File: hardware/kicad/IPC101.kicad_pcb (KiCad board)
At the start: 2 copper layers, 100 x 140 mm, 18 parts, among them J1 IPC-100 J10, J3 STOP J8A ONLY, SW1 START, SW2 PULL, SW3 NAV 5-WAY - VERIFY, U1 TCA8418RTWR

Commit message: Update IPC-101 for 2.42-inch OLED
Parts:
- removed DS1: ADAFRUIT 938 - J6 HARNESS, IPC101:OLED_MOUNT
- C1: value 100n -> 100nF
- C2: value 4.7u -> 4.7uF
- J3: value STOP J8A ONLY -> IPC-100 J8A STOP
- SW1: value START -> START B3F-4055
- SW2: value PULL -> PULL B3F-4055
- SW3: value NAV 5-WAY - VERIFY -> ADAFRUIT 504 - VERIFY PIN MAP
- TP1: value 3V3 -> +3V3
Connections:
- net +3V3 renamed /+3V3
- net C0 renamed /C0
- net GND renamed /GND
- net INT_TEST renamed /INT_TEST
- net R0_LEFT renamed /R0_LEFT
- net R1_RIGHT renamed /R1_RIGHT
- net R2_UP renamed /R2_UP
- net R3_DOWN renamed /R3_DOWN
- net R4_SELECT renamed /R4_SELECT
- net R5_START renamed /R5_START
- net R6_PULL renamed /R6_PULL
- net RESET renamed /RESET
- net SCL renamed /SCL
- net SDA renamed /SDA
- net STOP_IN_RAW renamed /STOP_IN_RAW
- net STOP_RETURN renamed /STOP_RETURN
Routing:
- net (no net): track 0.00 -> 430.0 mm
- net /C0: track 86.9 -> 0.00 mm
- net /SCL: track 66.3 -> 0.00 mm
- net /SDA: track 66.2 -> 0.00 mm
- net /+3V3: track 60.2 -> 0.00 mm
- net /R6_PULL: track 43.4 -> 0.00 mm
- net /R5_START: track 29.0 -> 0.00 mm
- net /R2_UP: track 19.4 -> 0.00 mm
- net /R1_RIGHT: track 16.4 -> 0.00 mm
- net /R0_LEFT: track 15.8 -> 0.00 mm
- net /R4_SELECT: track 11.0 -> 0.00 mm
- net /R3_DOWN: track 9.19 -> 0.00 mm
- net /GND: track 6.22 -> 0.00 mm

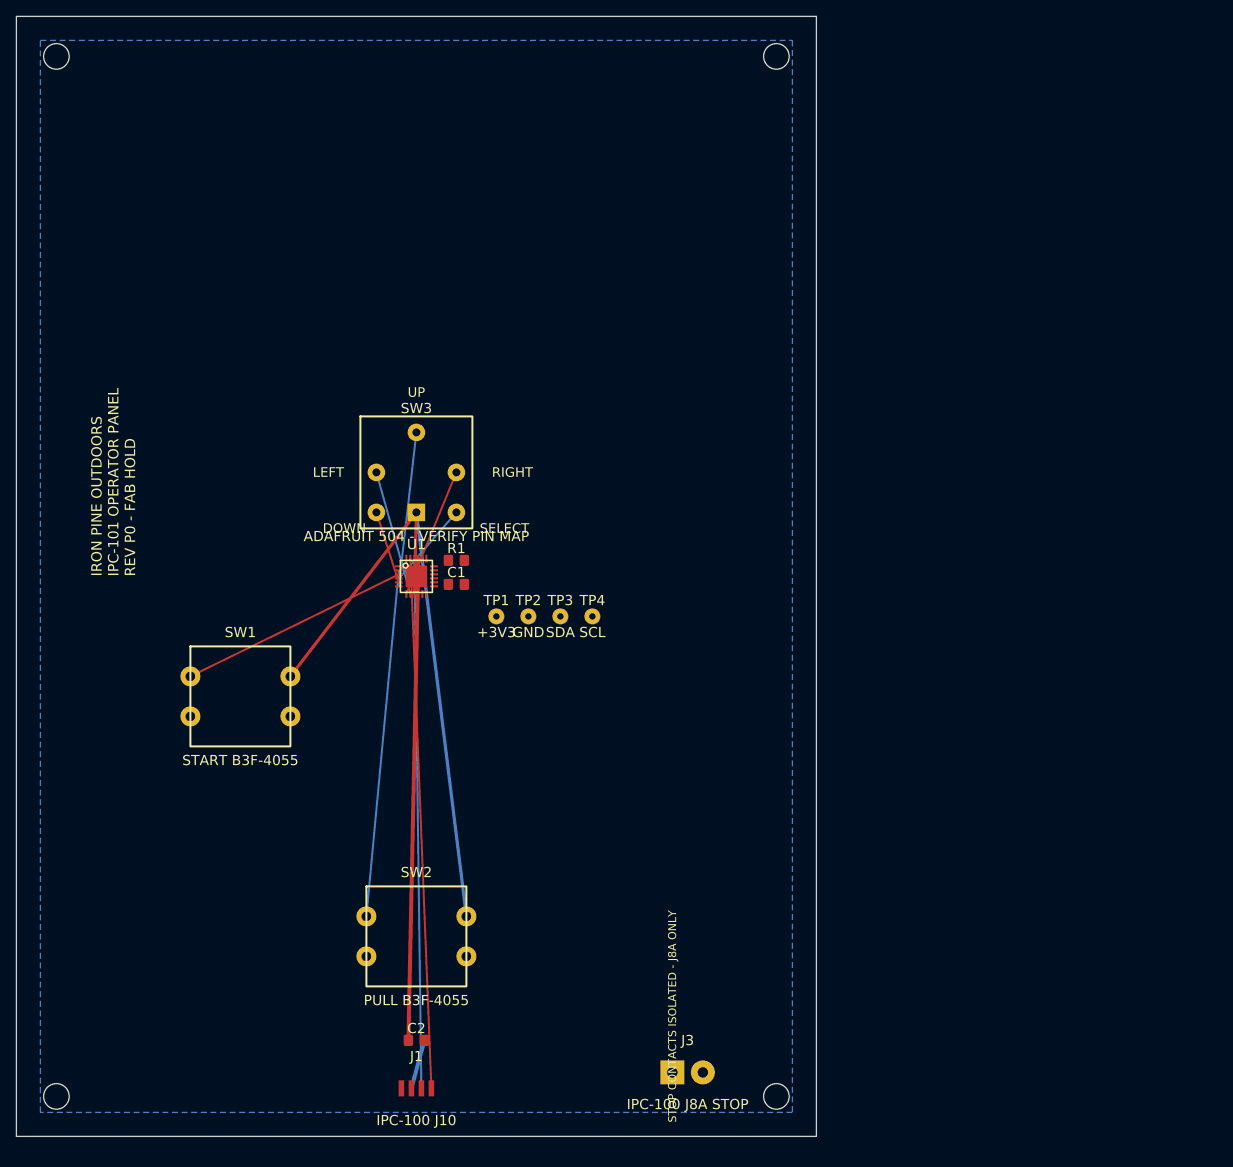
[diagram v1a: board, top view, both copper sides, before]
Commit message: Repair IPC-101 PCB routing
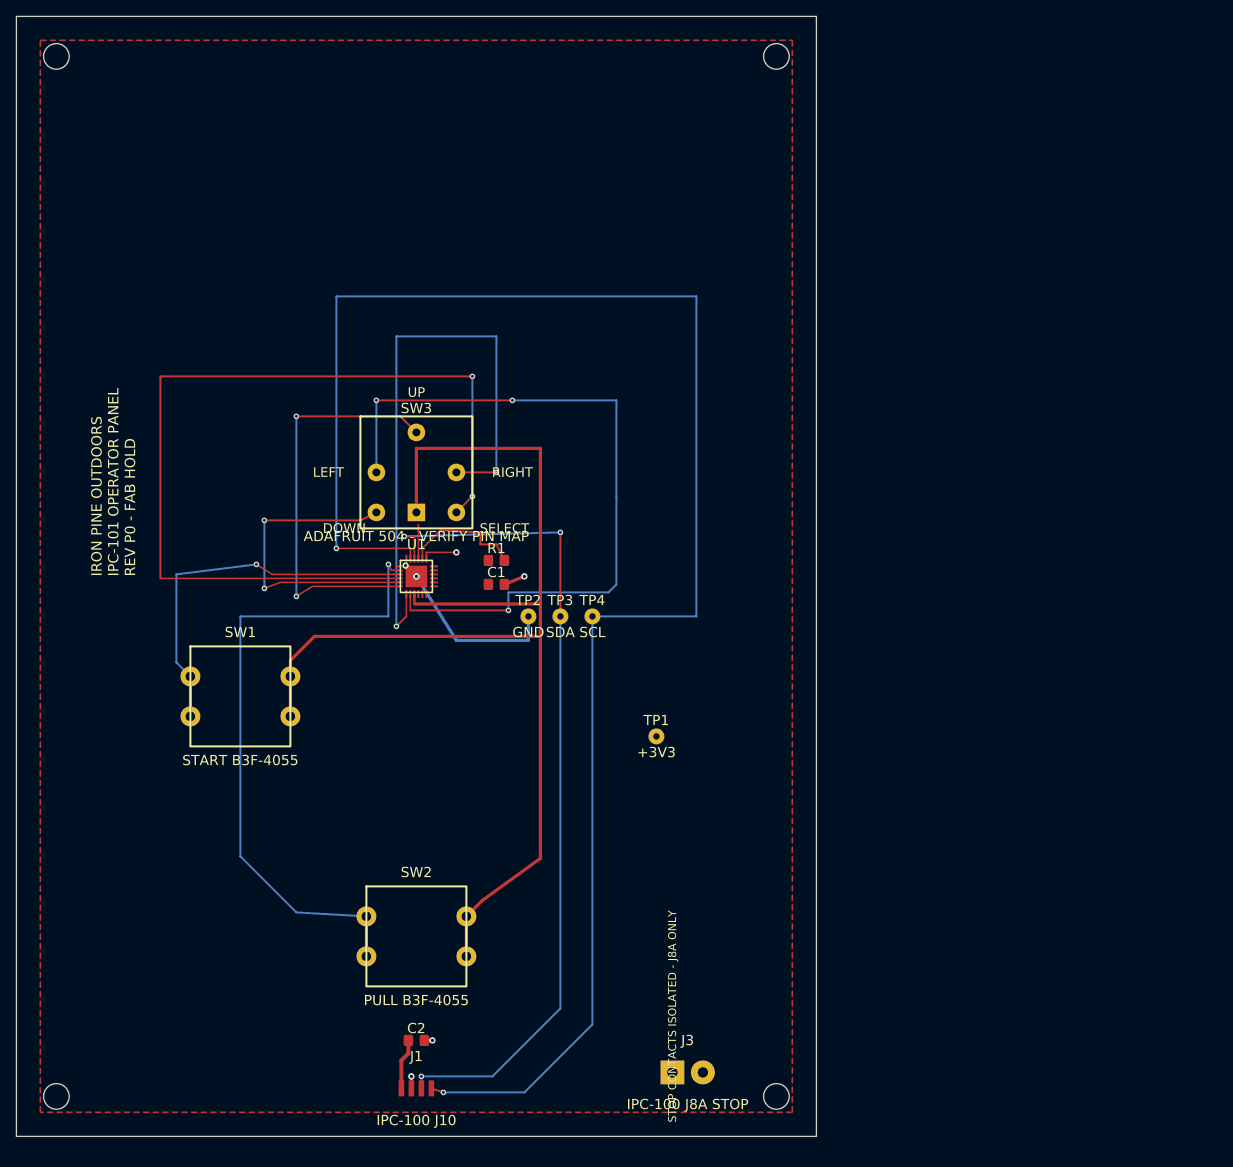
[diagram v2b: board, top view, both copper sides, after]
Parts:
- moved TP1 25.0 mm to (80.0, 90.0)
- moved C1 5.00 mm to (60.0, 71.0)
- moved R1 5.00 mm to (60.0, 68.0)
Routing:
- net (no net): track 430.0 -> 0.00 mm
- net /SCL: track 0.00 -> 214.8 mm, vias 0 -> 2
- net /C0: track 0.00 -> 148.0 mm
- net /R4_SELECT: track 0.00 -> 111.9 mm, vias 0 -> 2
- net /SDA: track 0.00 -> 105.5 mm, vias 0 -> 3
- net /R0_LEFT: track 0.00 -> 92.5 mm, vias 0 -> 3
- net /R6_PULL: track 0.00 -> 80.4 mm, vias 0 -> 1
- net /R1_RIGHT: track 0.00 -> 75.3 mm, vias 0 -> 2
- net /R2_UP: track 0.00 -> 51.5 mm, vias 0 -> 2
- net /R5_START: track 0.00 -> 46.7 mm, vias 0 -> 1
- net /R3_DOWN: track 0.00 -> 39.7 mm, vias 0 -> 2
- net /GND: track 0.00 -> 31.2 mm, vias 0 -> 5
- net /RESET: track 0.00 -> 15.2 mm
- net /+3V3: track 0.00 -> 10.7 mm
- added copper zone on F.Cu, net /+3V3

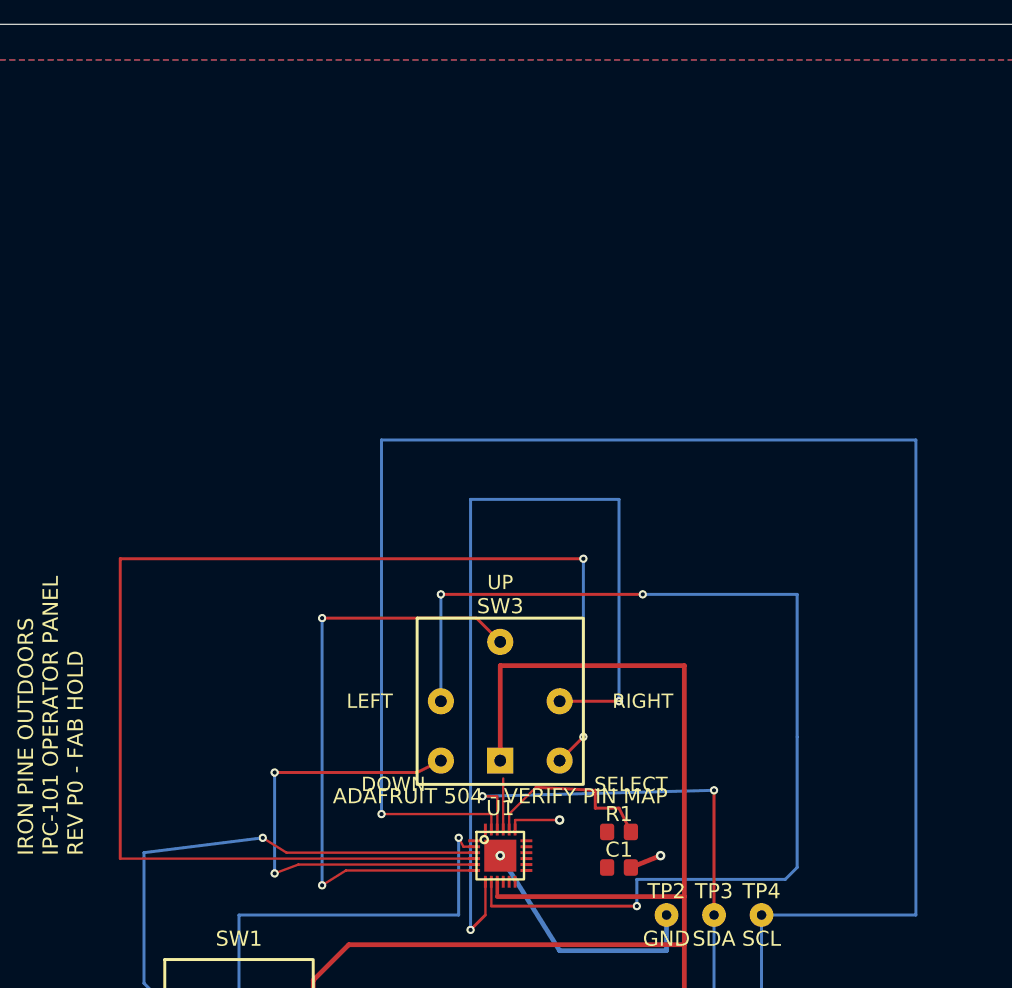
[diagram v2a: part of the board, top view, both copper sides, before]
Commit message: Mount 2.42 inch OLED on IPC-101
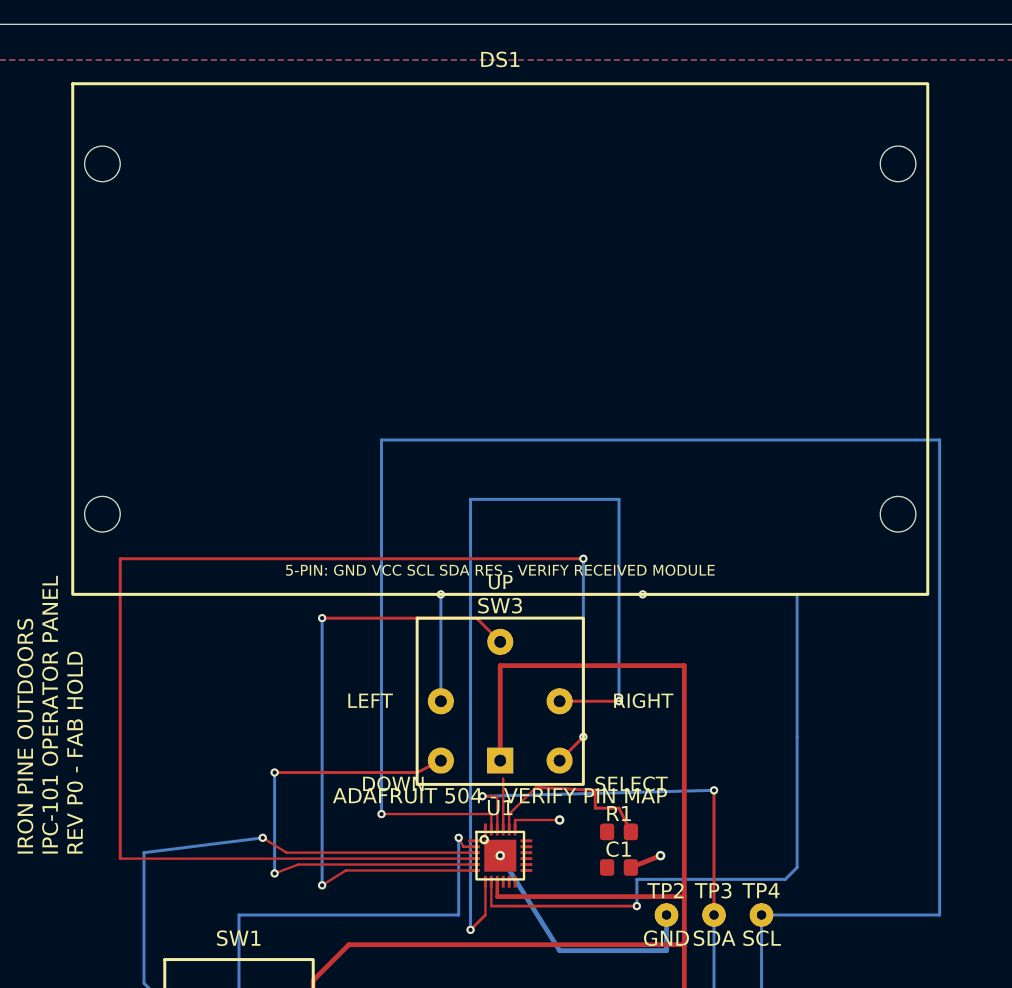
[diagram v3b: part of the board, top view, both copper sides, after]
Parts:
- added DS1: HOSYOND 2.42in SSD1309 - 5 WIRE J6 HARNESS, IPC101:HOSYOND_2.42_SSD1309_MOUNT, F.Cu at (50.0, 26.5)
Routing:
- net /SCL: track 214.8 -> 218.8 mm
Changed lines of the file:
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@@
+		(embedded_fonts no)
+	)
+	(footprint "IPC101:HOSYOND_2.42_SSD1309_MOUNT"
+		(layer "F.Cu")
+		(at 50 26.5)
+		(property "Reference" "DS1"
+			(at 0 -23.5 0)
+			(layer "F.SilkS")
+			(effects
+				(font
+					(size 1.27 1.27)
+				)
+			)
+		)
+		(property "Value" "HOSYOND 2.42in SSD1309 - 5 WIRE J6 HARNESS"
+			(at 0 23.5 0)
+			(layer "F.Fab")
+			(effects
+				(font
+					(size 1.27 1.27)
+				)
+			)
+		)
+		(property "Datasheet" ""
+			(at 0 0 0)
+			(layer "F.Fab")
+			(hide yes)
+			(effects
+				(font
+					(size 1.27 1.27)
+				)
+			)
+		)
+		(property "Description" ""
+			(at 0 0 0)
+			(layer "F.Fab")
+			(hide yes)
+			(effects
+				(font
+					(size 1.27 1.27)
+				)
+			)
+		)
+		(attr through_hole)
+		(duplicate_pad_numbers_are_jumpers no)
+		(fp_rect
+			(start -36 -21.5)
+			(end 36 21.5)
+			(stroke
+				(width 0.25)
+				(type default)
+			)
+			(fill no)
+			(layer "F.SilkS")
+		)
+		(fp_rect
+			(start -27.505 -13.745)
+			(end 27.505 13.745)
+			(stroke
+				(width 0.2)
+				(type default)
+			)
+			(fill no)
+			(layer "Dwgs.User")
+		)
+		(fp_rect
+			(start -30.25 -18.5)
+			(end 30.25 18.5)
+			(stroke
+				(width 0.15)
+				(type default)
+			)
+			(fill no)
+			(layer "F.Fab")
+		)
+		(fp_text user "5-PIN: GND VCC SCL SDA RES - VERIFY RECEIVED MODULE"
+			(at 0 19.5 0)
+			(layer "F.SilkS")
+			(effects
+				(font
+					(size 0.9 0.9)
+					(thickness 0.14)
+				)
+			)
+		)
+		(fp_text user "ACTIVE AREA 55.01 x 27.49"
+			(at 0 0 0)
+			(layer "Dwgs.User")
+			(effects
+				(font
+					(size 1 1)
+					(thickness 0.15)
+				)
+			)
+		)
+		(pad "" np_thru_hole circle
+			(at -33.5 -14.75)
+			(size 3 3)
+			(drill 3)
+			(layers "*.Cu" "*.Mask")
+		)
+		(pad "" np_thru_hole circle
+			(at -33.5 14.75)
+			(size 3 3)
+			(drill 3)
+			(layers "*.Cu" "*.Mask")
+		)
+		(pad "" np_thru_hole circle
+			(at 33.5 -14.75)
+			(size 3 3)
+			(drill 3)
+			(layers "*.Cu" "*.Mask")
+		)
+		(pad "" np_thru_hole circle
+			(at 33.5 14.75)
+			(size 3 3)
+			(drill 3)
+			(layers "*.Cu" "*.Mask")
+		)
 		(embedded_fonts no)
 	)
@@
 	(segment
 		(start 40 35)
-		(end 85 35)
+		(end 87 35)
 		(width 0.25)
 		(layer "B.Cu")
@@
 	)
 	(segment
-		(start 85 35)
-		(end 85 75)
+		(start 87 35)
+		(end 87 75)
 		(width 0.25)
 		(layer "B.Cu")
@@
 	)
 	(segment
-		(start 85 75)
+		(start 87 75)
 		(end 72 75)
 		(width 0.25)

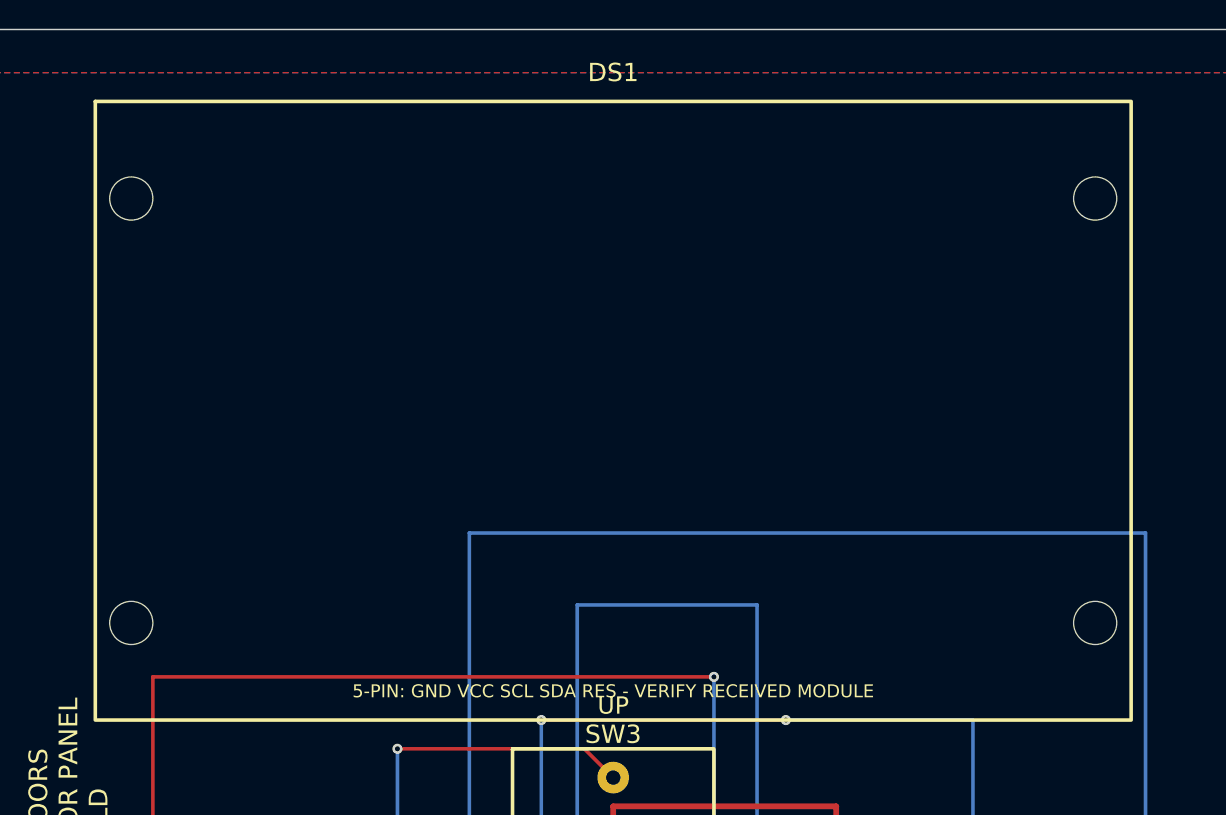
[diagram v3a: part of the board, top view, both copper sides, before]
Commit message: Use Crosswind OLED mounting geometry
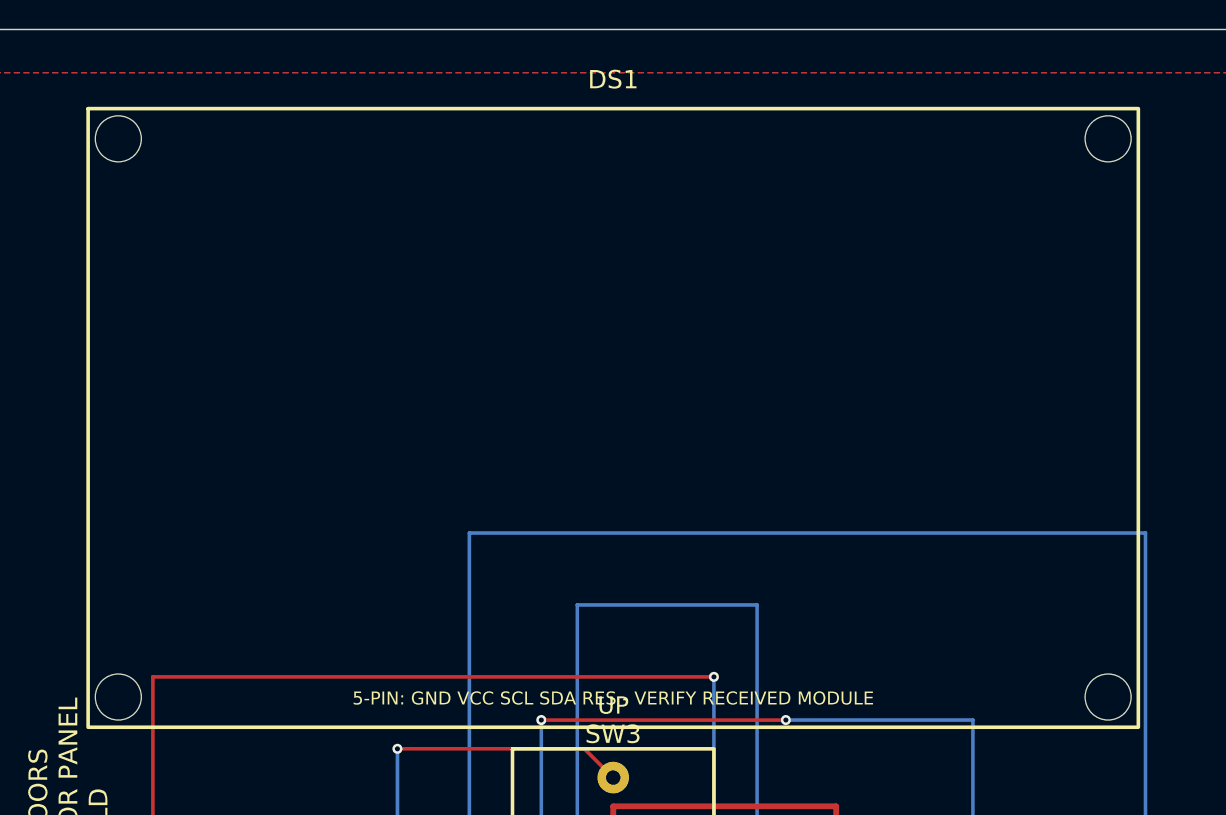
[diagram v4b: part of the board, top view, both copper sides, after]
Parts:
- moved DS1 0.50 mm to (50.0, 27.0)
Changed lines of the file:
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@@
 	(footprint "IPC101:HOSYOND_2.42_SSD1309_MOUNT"
 		(layer "F.Cu")
-		(at 50 26.5)
+		(at 50 27)
 		(property "Reference" "DS1"
 			(at 0 -23.5 0)
@@
 		(duplicate_pad_numbers_are_jumpers no)
 		(fp_rect
-			(start -36 -21.5)
-			(end 36 21.5)
+			(start -36.5 -21.5)
+			(end 36.5 21.5)
 			(stroke
 				(width 0.25)
@@
 		)
 		(pad "" np_thru_hole circle
-			(at -33.5 -14.75)
-			(size 3 3)
-			(drill 3)
+			(at -34.4 -19.4)
+			(size 3.2 3.2)
+			(drill 3.2)
 			(layers "*.Cu" "*.Mask")
 		)
 		(pad "" np_thru_hole circle
-			(at -33.5 14.75)
-			(size 3 3)
-			(drill 3)
+			(at -34.4 19.4)
+			(size 3.2 3.2)
+			(drill 3.2)
 			(layers "*.Cu" "*.Mask")
 		)
 		(pad "" np_thru_hole circle
-			(at 33.5 -14.75)
-			(size 3 3)
-			(drill 3)
+			(at 34.4 -19.4)
+			(size 3.2 3.2)
+			(drill 3.2)
 			(layers "*.Cu" "*.Mask")
 		)
 		(pad "" np_thru_hole circle
-			(at 33.5 14.75)
-			(size 3 3)
-			(drill 3)
+			(at 34.4 19.4)
+			(size 3.2 3.2)
+			(drill 3.2)
 			(layers "*.Cu" "*.Mask")
 		)
